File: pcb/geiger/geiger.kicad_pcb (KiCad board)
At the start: 2 copper layers, 160 x 112.4 mm, 103 parts, among them J1 Conn_01x02, J2 Conn_01x02, J3 Conn_01x03, J4 Conn_01x06, J5 Conn_01x02, J6 Conn_02x05_Odd_Even, J7 Conn_02x05_Odd_Even, K1 RELAY_DPST, K2 RELAY_DPST, Q1 BC107, Q2 BC211, Q3 BC313, Q4 IRF540N, Q5 BC140, Q6 BC140, Q7 BC307, Q8 BC847, Q9 BC847, U1 MSP430G2553_PW20, U2 74HC595, U3 AD558, U4 LM208, X1 5.7MHz

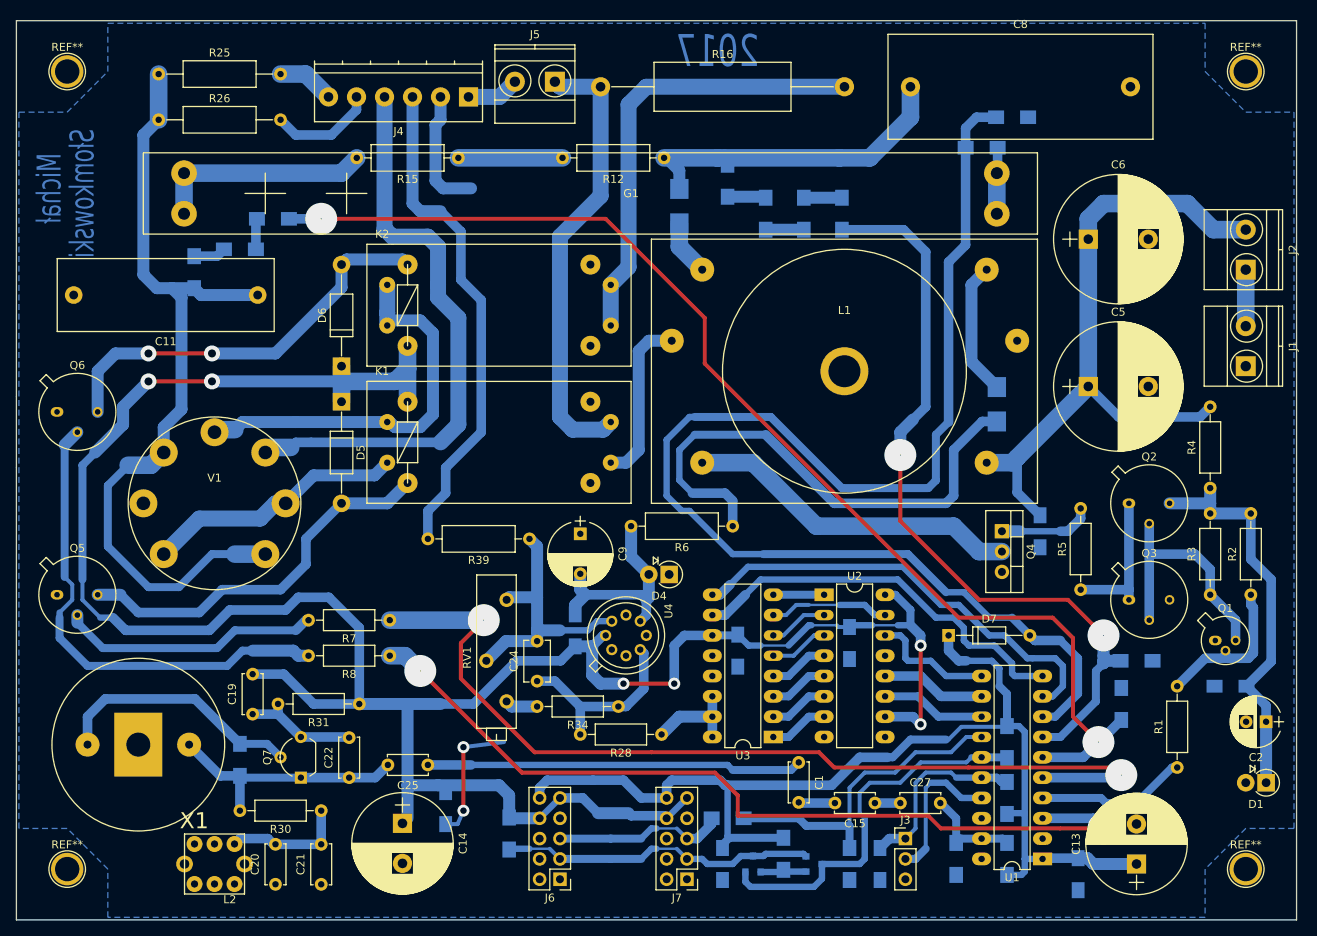
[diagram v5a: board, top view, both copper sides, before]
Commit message: Add ready schematic and all connections on board.
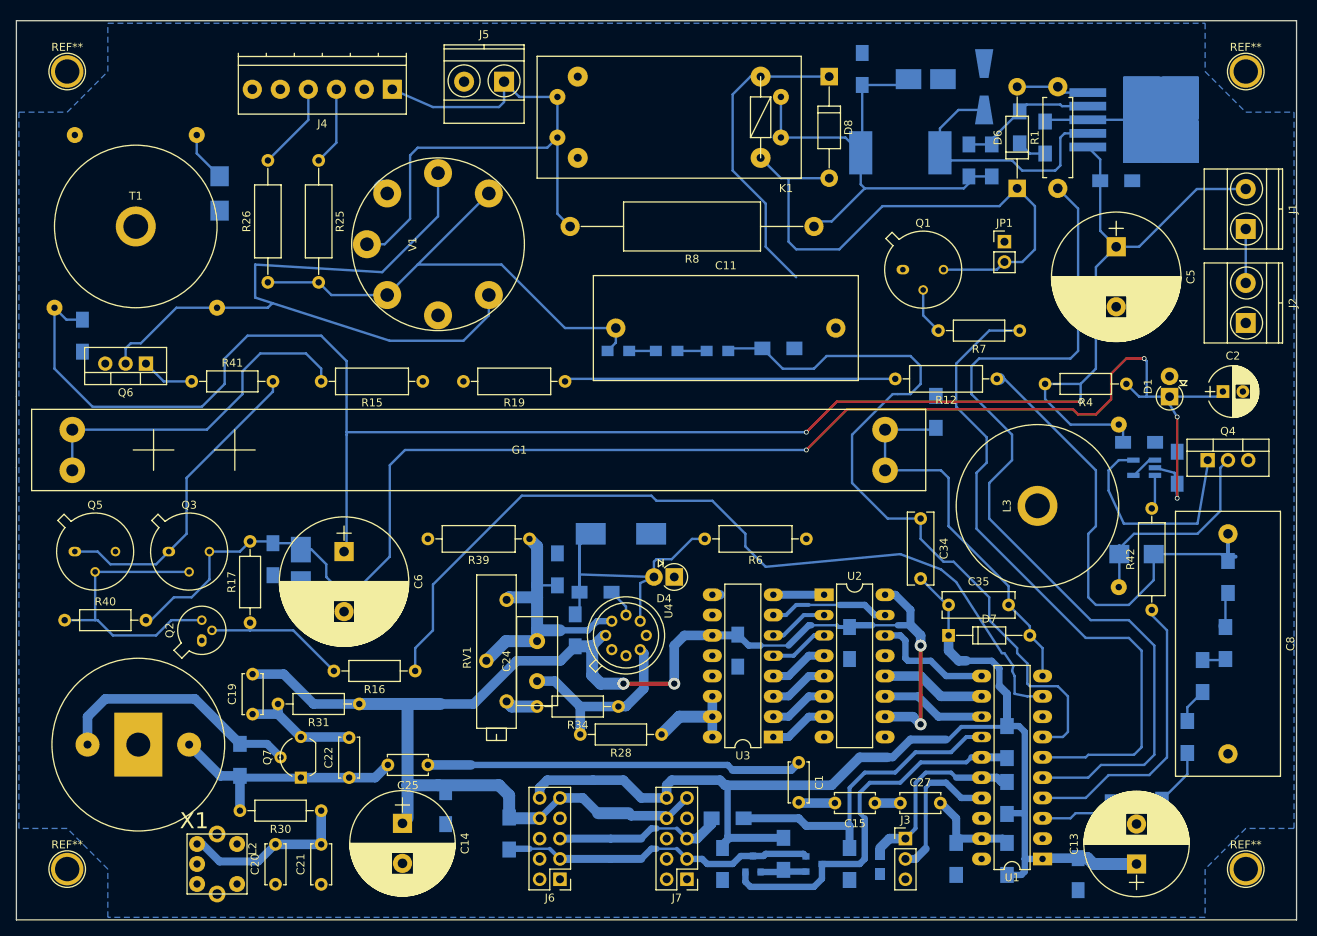
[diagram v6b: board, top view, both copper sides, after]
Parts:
- removed K2: RELAY_DPST, RELAY_DPST_Telfa_K-8:RELAY_DPST_Telfa_K-8
- added C17: 10n, Capacitors_SMD:C_1206_HandSoldering, B.Cu at (135.3, 33.3)
- added C28: 22u, Capacitors_Tantalum_SMD:CP_Tantalum_Case-B_EIA-3528-21_Hand, B.Cu at (129.9, 23.2)
- added C29: 100n, Capacitors_SMD:C_1206_HandSoldering, B.Cu at (121.9, 21.9)
- added C30: 100n, Capacitors_SMD:C_1206_HandSoldering, B.Cu at (48.3, 83.2)
- added C31: 100n, Capacitors_SMD:C_1206_HandSoldering, B.Cu at (24.4, 55.2)
- added C32: 100n, Capacitors_SMD:C_1206_HandSoldering, B.Cu at (161.3, 71.8)
- added C33: 10n, Capacitors_SMD:C_1206_HandSoldering, B.Cu at (153.0, 115.6)
- added C34: 10n, Capacitors_ThroughHole:C_Rect_L9.0mm_W3.2mm_P7.50mm_MKT, F.Cu at (129.2, 78.1)
- added C35: 33p, Capacitors_ThroughHole:C_Rect_L9.0mm_W3.2mm_P7.50mm_MKT, F.Cu at (132.7, 88.9)
- added C36: 100n, Capacitors_SMD:C_1206_HandSoldering, B.Cu at (88.6, 87.3)
- added C37: 100n, Capacitors_SMD:C_1206_HandSoldering, B.Cu at (83.8, 84.5)
- added C38: 22u, Capacitors_Tantalum_SMD:CP_Tantalum_Case-B_EIA-3528-21_Hand, B.Cu at (51.8, 84.1)
- added D8: D, Diodes_ThroughHole:D_DO-41_SOD81_P12.70mm_Horizontal, F.Cu at (117.8, 22.9)
- added JP1: Jumper, Pin_Headers:Pin_Header_Straight_1x02_Pitch2.54mm, F.Cu at (139.7, 43.5)
- added L3: L_Core_Ferrite, F1001:F1001_coil, F.Cu at (143.8, 76.5)
- added R17: 56k, Resistors_ThroughHole:R_Axial_DIN0207_L6.3mm_D2.5mm_P10.16mm_Horizontal, F.Cu at (45.4, 91.1)
- added R40: 3k3, Resistors_ThroughHole:R_Axial_DIN0207_L6.3mm_D2.5mm_P10.16mm_Horizontal, F.Cu at (22.2, 90.8)
- added R41: 1R7, Resistors_ThroughHole:R_Axial_DIN0207_L6.3mm_D2.5mm_P10.16mm_Horizontal, F.Cu at (38.1, 61.0)
- added R42: 100, Resistors_ThroughHole:R_Axial_DIN0309_L9.0mm_D3.2mm_P12.70mm_Horizontal, F.Cu at (158.1, 89.5)
- added T1: Transformer_1P_1S, F1001:F1001_trans, F.Cu at (31.1, 41.6)
- added U5: LM2596, TO_SOT_Packages_SMD:TO-263-5_TabPin3, B.Cu at (155.9, 28.3)
- added U6: MCP1402, TO_SOT_Packages_SMD:SOT-23-5_HandSoldering, B.Cu at (157.2, 71.8)
- C10: footprint Capacitors_SMD:C_1206_HandSoldering -> Capacitors_SMD:C_0805_HandSoldering
- C11: value 470n -> 2u2; footprint Capacitors_ThroughHole:C_Rect_L27.0mm_W9.0mm_P23.00mm -> Capacitors_ThroughHole:C_Rect_L33.0mm_W13.0mm_P27.50mm_MKS4
- C13, C14: footprint Capacitors_ThroughHole:CP_Radial_D12.5mm_P5.00mm -> Capacitors_ThroughHole:CP_Radial_D13.0mm_P5.00mm
- C2: value 100u -> 4u7
- C24: value 10n -> 33n; footprint Capacitors_ThroughHole:C_Disc_D5.1mm_W3.2mm_P5.00mm -> Capacitors_ThroughHole:C_Disc_D11.0mm_W5.0mm_P5.00mm
- C9: value 47u -> 6u8; footprint Capacitors_ThroughHole:CP_Radial_D8.0mm_P5.00mm -> Capacitors_Tantalum_SMD:CP_Tantalum_Case-D_EIA-7343-31_Hand; moved to B.Cu
- D5: value D -> SS34; footprint Diodes_ThroughHole:D_DO-41_SOD81_P12.70mm_Horizontal -> Diodes_SMD:D_SMA-SMB_Universal_Handsoldering; moved to B.Cu
- L1: value FLYBACK_TRANS -> L_Core_Ferrite; footprint FLYBACK_TRANS:FLYBACK_TRANS -> Choke_SMD:Choke_SMD_12x12mm_h8mm; moved to B.Cu
- L2: footprint L_7x7:L_7x7 -> L_7x7:L_7x7_II
- Q1: value BC107 -> BC140; footprint TO_SOT_Packages_THT:TO-18-3 -> TO_SOT_Packages_THT:TO-39-3
- Q2: value BC211 -> BC107; footprint TO_SOT_Packages_THT:TO-39-3 -> TO_SOT_Packages_THT:TO-18-3
- Q3: value BC313 -> BC211
- Q5: value BC140 -> BC313
- Q6: value BC140 -> IRF540N; footprint TO_SOT_Packages_THT:TO-39-3 -> TO_SOT_Packages_THT:TO-220-3_Vertical
- R1: value 1k5 -> 1k; footprint Resistors_ThroughHole:R_Axial_DIN0207_L6.3mm_D2.5mm_P10.16mm_Horizontal -> Resistors_ThroughHole:R_Axial_DIN0411_L9.9mm_D3.6mm_P12.70mm_Horizontal
- R12: value 1M -> 1M6
- R15: value 2M2 -> 1M6
- R16: value 10 -> 1k5; footprint Resistors_ThroughHole:R_Axial_DIN0617_L17.0mm_D6.0mm_P30.48mm_Horizontal -> Resistors_ThroughHole:R_Axial_DIN0207_L6.3mm_D2.5mm_P10.16mm_Horizontal
- R19: footprint Resistors_SMD:R_1206_HandSoldering -> Resistors_ThroughHole:R_Axial_DIN0309_L9.0mm_D3.2mm_P12.70mm_Horizontal; moved to F.Cu
- R2: value 56k -> 3k9; footprint Resistors_ThroughHole:R_Axial_DIN0207_L6.3mm_D2.5mm_P10.16mm_Horizontal -> Resistors_SMD:R_1206_HandSoldering; moved to B.Cu
- R21, R22, R23: footprint Resistors_SMD:R_1206_HandSoldering -> Resistors_SMD:R_0805_HandSoldering
- R25: value 100k -> 510k
- R26: value 100k -> 10k
- R3: value 3k3 -> 3k9; footprint Resistors_ThroughHole:R_Axial_DIN0207_L6.3mm_D2.5mm_P10.16mm_Horizontal -> Resistors_SMD:R_1206_HandSoldering; moved to B.Cu
- R34: value 47k -> 22k
- R5: value 1R7 -> 3k9; footprint Resistors_ThroughHole:R_Axial_DIN0207_L6.3mm_D2.5mm_P10.16mm_Horizontal -> Resistors_SMD:R_1206_HandSoldering; moved to B.Cu
- R8: value 1k -> 10; footprint Resistors_ThroughHole:R_Axial_DIN0207_L6.3mm_D2.5mm_P10.16mm_Horizontal -> Resistors_ThroughHole:R_Axial_DIN0617_L17.0mm_D6.0mm_P30.48mm_Horizontal
- U4: value LM208 -> MAA725
- moved Q3 120.2 mm to (35.2, 82.2)
- moved Q2 117.1 mm to (39.4, 93.3), turned to 90 degrees
- moved C6 100.9 mm to (57.1, 82.2), turned to 270 degrees
- moved D2 100.7 mm to (41.6, 37.5)
- moved D5 89.5 mm to (137.2, 24.1), turned to 90 degrees
- moved D6 87.3 mm to (141.3, 36.8)
- moved R7 86.7 mm to (141.6, 54.6)
- moved R9 79.8 mm to (167.6, 85.4)
- moved R11 78.6 mm to (167.3, 93.7)
- moved R14 78.4 mm to (162.6, 105.4)
- moved R16 76.6 mm to (66.0, 97.2), turned to 180 degrees
- moved R13 76.3 mm to (164.5, 97.8), turned to 270 degrees
- moved R8 75.4 mm to (115.9, 41.6)
- moved R1 73.9 mm to (146.4, 36.8)
- moved D3 71.8 mm to (156.2, 82.5), turned to 180 degrees
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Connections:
- C2 pad 1: Net-(C2-Pad1) -> +15V
- C4 pad 1: Net-(C2-Pad1) -> +36V
- C5 pad 1: Net-(C5-Pad1) -> +36V
- C6 pad 1: Net-(C5-Pad1) -> +36V
- C7 pad 1: GND -> +36V
- C7 pad 2: Net-(C5-Pad1) -> GND
- D1 pad 1: Net-(C2-Pad1) -> +15V
- D5 pad 1: +5V -> Net-(D5-Pad1)
- D5 pad 2: Net-(D5-Pad2) -> GND
- D6 pad 1: +5V -> Net-(D6-Pad1)
- G1 pad K: Net-(G1-PadK) -> GM_PULSE
- J1 pad 1: GND -> Net-(J1-Pad1)
- J1 pad 2: Net-(J1-Pad2) -> +36V
- J2 pad 1: Net-(J1-Pad2) -> GND
- J2 pad 2: Net-(C5-Pad1) -> Net-(J1-Pad1)
- J4 pad 1: Net-(J4-Pad1) -> HEATER_6_3V
- J4 pad 3: EYE_GRID -> Net-(J4-Pad3)
- J4 pad 5: Net-(J4-Pad5) -> (no net)
- J4 pad 6: Net-(J4-Pad6) -> EYE_GRID
- J5 pad 1: Net-(J5-Pad1) -> HEATER_6_3V
- J5 pad 2: Net-(J4-Pad1) -> GND
- J6 pad 4: Net-(J6-Pad4) -> (no net)
- J6 pad 6: Net-(J6-Pad6) -> (no net)
- J6 pad 7: Net-(J6-Pad7) -> (no net)
- J7 pad 4: Net-(J7-Pad4) -> (no net)
- J7 pad 6: Net-(J7-Pad6) -> (no net)
- J7 pad 7: Net-(J7-Pad7) -> (no net)
- K1 pad 1: +5V -> Net-(D6-Pad1)
- K1 pad 2: Net-(D5-Pad2) -> +5V
- K1 pad 5: Net-(K1-Pad5) -> Net-(C17-Pad1)
- K1 pad 6: Net-(K1-Pad6) -> HEATER_6_3V
- K1 pad 7: Net-(K1-Pad7) -> Net-(C17-Pad1)
- K1 pad 8: Net-(J5-Pad1) -> HEATER_6_3V
- L1 pad 1: Net-(C5-Pad1) -> Net-(D5-Pad1)
- L1 pad 2: Net-(L1-Pad2) -> Net-(C17-Pad1)
- Q1 pad 3: Net-(Q1-Pad3) -> Net-(D6-Pad1)
- Q2 pad 1: Net-(Q2-Pad1) -> GND
- Q2 pad 2: Net-(Q1-Pad3) -> Net-(Q2-Pad2)
- Q2 pad 3: Net-(C2-Pad1) -> Net-(Q2-Pad3)
- Q3 pad 1: Net-(Q2-Pad1) -> Net-(Q3-Pad1)
- Q3 pad 2: Net-(Q1-Pad3) -> Net-(Q2-Pad3)
- Q3 pad 3: GND -> +15V
- Q4 pad 2: Net-(L1-Pad2) -> Net-(D3-Pad2)
- Q5 pad 1: GND -> Net-(Q3-Pad1)
- Q5 pad 2: Net-(Q5-Pad2) -> Net-(Q2-Pad3)
- Q5 pad 3: Net-(D5-Pad2) -> GND
- Q6 pad 1: GND -> Net-(Q6-Pad1)
- Q6 pad 3: Net-(D6-Pad2) -> GND
- R1 pad 1: FLYBACK_PULSE -> HEATER1
- R1 pad 2: Net-(Q1-Pad2) -> Net-(D6-Pad2)
- R15 pad 1: Net-(R12-Pad2) -> Net-(R15-Pad1)
- R16 pad 1: Net-(J5-Pad1) -> EYE_PWM
- R16 pad 2: Net-(K2-Pad6) -> Net-(Q2-Pad2)
- R19 pad 1: Net-(G1-PadK) -> Net-(R12-Pad2)
- R19 pad 2: GM_PULSE -> Net-(R15-Pad1)
- R2 pad 1: Net-(Q1-Pad2) -> Net-(C17-Pad2)
- R2 pad 2: Net-(C2-Pad1) -> Net-(R2-Pad2)
- R21 pad 1: Net-(C11-Pad1) -> Net-(R21-Pad1)
- R21 pad 2: Net-(R21-Pad2) -> Net-(C11-Pad1)
- R22 pad 2: Net-(R21-Pad2) -> Net-(R21-Pad1)
- R23 pad 1: Net-(R22-Pad1) -> EYE_VOL
- R23 pad 2: EYE_VOL -> Net-(R22-Pad1)
- R25 pad 1: Net-(C11-Pad1) -> Net-(J4-Pad3)
- R25 pad 2: Net-(J4-Pad6) -> Net-(C11-Pad1)
- R26 pad 2: Net-(J4-Pad5) -> Net-(J4-Pad4)
- R3 pad 1: Net-(Q1-Pad3) -> Net-(C17-Pad1)
- R3 pad 2: Net-(C2-Pad1) -> Net-(C17-Pad2)
- R4 pad 1: Net-(C2-Pad1) -> +15V
- R4 pad 2: Net-(C5-Pad1) -> +36V
- R5 pad 1: Net-(Q2-Pad1) -> Net-(R2-Pad2)
- R5 pad 2: Net-(Q4-Pad1) -> GND
- R7 pad 1: REL_HEATER_2 -> HEATER2
- R7 pad 2: Net-(Q5-Pad2) -> Net-(Q1-Pad2)
- R8 pad 1: REL_HEATER_1 -> Net-(C17-Pad1)
- R8 pad 2: Net-(Q6-Pad2) -> HEATER_6_3V
- U1 pad 10: DAC_CS -> GM_PULSE
- U1 pad 18: Net-(U1-Pad18) -> (no net)
- U1 pad 2: Net-(U1-Pad2) -> (no net)
- U1 pad 3: REL_HEATER_1 -> GM_VOL
- U1 pad 4: FLYBACK_PULSE -> GM_PWM
- U1 pad 5: REL_HEATER_2 -> HEATER1
- U1 pad 6: EYE_VOL -> HEATER2
- U1 pad 7: GM_VOL -> EYE_VOL
- U1 pad 8: GM_PULSE -> (no net)
- U1 pad 9: DAC_CE -> EYE_PWM
- U2 pad 9: Net-(U2-Pad9) -> (no net)
- U3 pad 10: DAC_CS -> GND
- U3 pad 9: DAC_CE -> GND
- U4 pad 1: Net-(U4-Pad1) -> (no net)
- U4 pad 8: Net-(U4-Pad8) -> (no net)
- V1 pad 2: Net-(K1-Pad5) -> Net-(Q6-Pad2)
- V1 pad 3: Net-(J4-Pad4) -> GND
- V1 pad 4: Net-(K1-Pad7) -> HEATER_6_3V
- V1 pad 6: Net-(V1-Pad6) -> (no net)
- V1 pad 7: Net-(K1-Pad5) -> Net-(Q6-Pad2)
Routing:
- net +36V: track 0.00 -> 248.6 mm, vias 0 -> 2
- net +15V: track 0.00 -> 193.2 mm, vias 0 -> 4
- net REL_HEATER_2: track 118.2 -> 0.00 mm, vias 2 -> 0
- net GM_PULSE: track 165.8 -> 49.8 mm
- net HEATER1: track 0.00 -> 113.9 mm
- net EYE_PWM: track 0.00 -> 107.9 mm
- net REL_HEATER_1: track 107.8 -> 0.00 mm, vias 2 -> 0
- net Net-(C5-Pad1): track 85.8 -> 0.00 mm
- net +5V: track 309.7 -> 224.3 mm, vias 6 -> 4
- net HEATER2: track 0.00 -> 84.3 mm
- net HEATER_6_3V: track 0.00 -> 76.9 mm
- net GM_VOL: track 98.0 -> 23.0 mm, vias 2 -> 0
- net Net-(D6-Pad1): track 0.00 -> 70.7 mm
- net Net-(D2-Pad2): track 66.3 -> 0.00 mm
- net EYE_GRID: track 63.1 -> 0.00 mm
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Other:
- board text removed: "2017"
- board text removed: "Michał"
- board text removed: "Słomkowski"

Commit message: All connections ready.
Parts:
- added C39: 6u8, Capacitors_Tantalum_SMD:CP_Tantalum_Case-D_EIA-7343-31_Hand, B.Cu at (21.0, 43.5)
- R41: footprint Resistors_ThroughHole:R_Axial_DIN0207_L6.3mm_D2.5mm_P10.16mm_Horizontal -> Resistors_ThroughHole:R_Axial_DIN0309_L9.0mm_D3.2mm_P12.70mm_Horizontal
- R42: footprint Resistors_ThroughHole:R_Axial_DIN0309_L9.0mm_D3.2mm_P12.70mm_Horizontal -> Resistors_ThroughHole:R_Axial_DIN0309_L9.0mm_D3.2mm_P15.24mm_Horizontal
- moved R6 89.9 mm to (42.5, 27.3)
- moved C9 78.1 mm to (33.0, 28.6), turned to 90 degrees
- moved C30 6.43 mm to (42.9, 86.7), turned to 0 degrees
- moved D3 6.33 mm to (162.2, 84.5), turned to 90 degrees
- moved R23 4.86 mm to (108.6, 58.1)
- moved R22 4.55 mm to (101.9, 58.1)
- moved R21 4.24 mm to (95.6, 58.1)
- moved D2 3.55 mm to (40.0, 34.3), turned to 0 degrees
- moved R24 2.93 mm to (114.3, 56.2), turned to 90 degrees
- moved R20 2.86 mm to (131.1, 67.6)
- moved R13 2.01 mm to (165.1, 99.7)
- moved J4 1.91 mm to (65.1, 24.4)
- moved R42 1.91 mm to (158.1, 91.4)
- moved C28 1.90 mm to (128.0, 23.2)
- moved D4 1.71 mm to (97.8, 83.8)
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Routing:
- net -VDC: track 44.3 -> 133.1 mm, vias 0 -> 2
- net EYE_GRID: track 0.00 -> 73.9 mm, vias 0 -> 2
- net +5V: track 224.3 -> 268.1 mm, vias 4 -> 6
- net HEATER1: track 113.9 -> 101.7 mm
- net HEATER2: track 84.3 -> 73.5 mm
- net HEATER_6_3V: track 76.9 -> 67.2 mm
- net +36V: track 248.6 -> 257.1 mm
- net Net-(Q6-Pad2): track 92.1 -> 99.8 mm
- net +15V: track 193.2 -> 200.8 mm
- net Net-(D2-Pad2): track 0.00 -> 7.15 mm
- net Net-(R15-Pad1): track 0.00 -> 4.13 mm
- net Net-(R12-Pad2): track 41.4 -> 45.0 mm
- net EYE_VOL: track 96.8 -> 93.3 mm
- net Net-(C8-Pad1): track 61.9 -> 58.8 mm
- net EYE_PWM: track 107.9 -> 104.9 mm
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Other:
- board text added: "Michał"
- board text added: "Słomkowski"

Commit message: Add every feature on the board. Beta.
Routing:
- net GND: track 20.6 -> 98.3 mm
- net -VDC: track 133.1 -> 140.1 mm
- net EYE_PWM: track 104.9 -> 108.1 mm
- net Net-(R12-Pad2): track 45.0 -> 43.7 mm
- net +36V: track 257.1 -> 256.0 mm
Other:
- board text added: "2018"
